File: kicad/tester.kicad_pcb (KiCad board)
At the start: 2 copper layers, 65 parts, among them J3 CONN_01X06, Q1 IRLML2402, Q2 IRLML6402, Q3 BC847, Q4 BC847, Q5 BC847, U2 NCP1450A, U3 ATMEGA328-AU, U4 LTC4054, U5 74LVC1G17, U6 SRV05, U7 XC6206P332, U8 MICRO-B_USB, Y1 16MHz

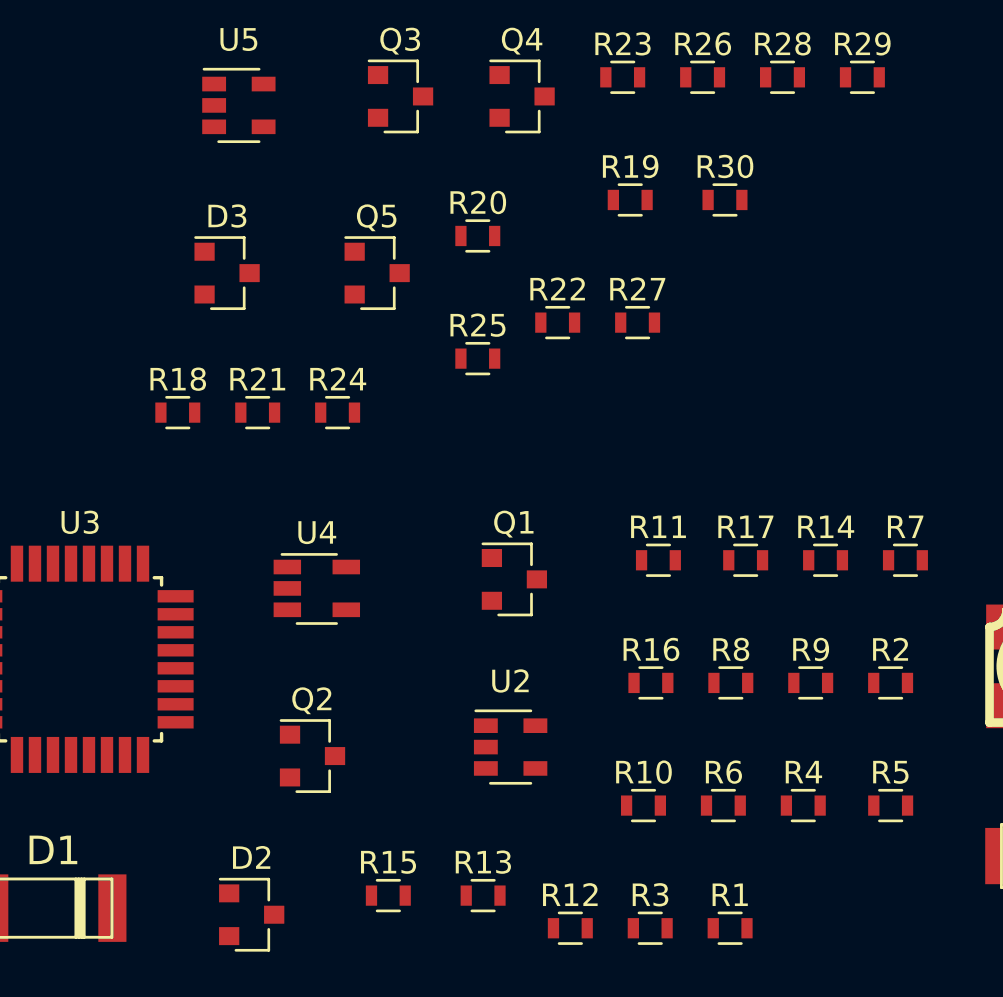
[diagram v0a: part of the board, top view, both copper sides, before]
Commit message: Change package some resistors
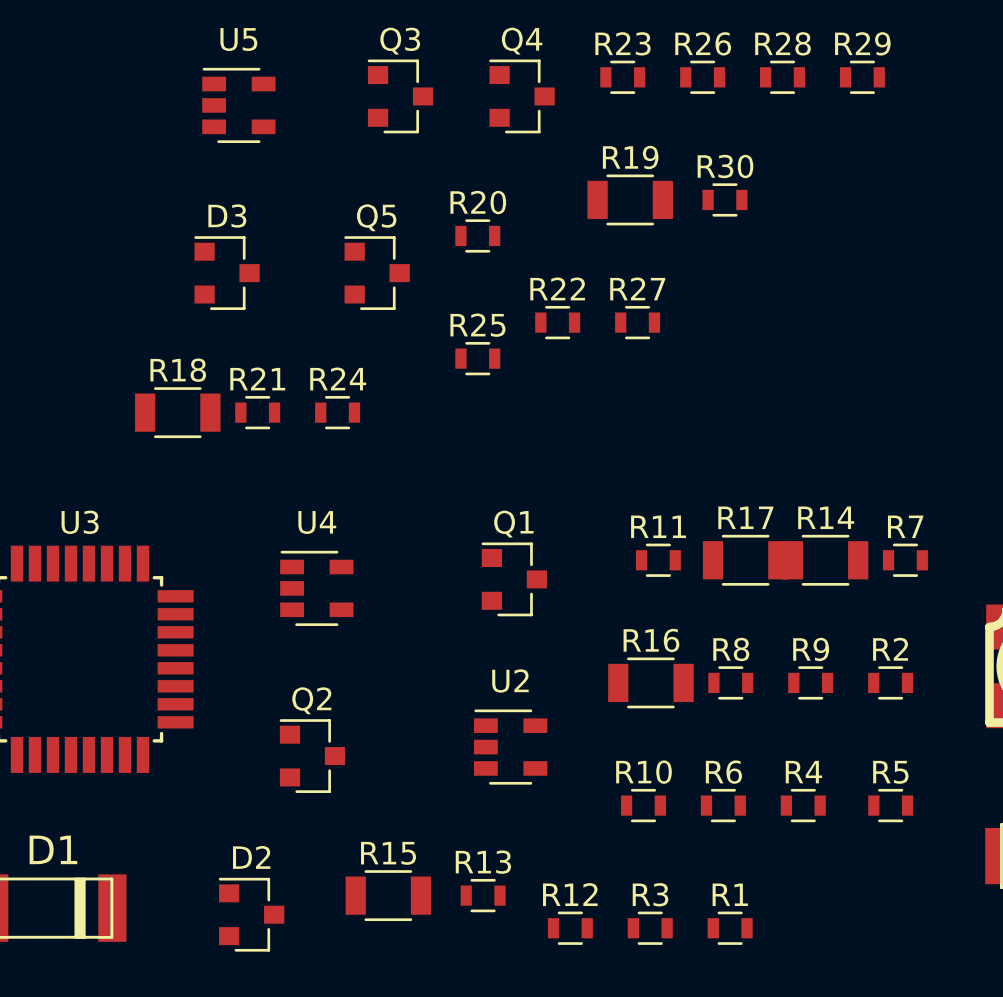
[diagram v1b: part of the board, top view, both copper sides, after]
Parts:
- R14, R15, R16, R17, R18, R19: footprint Resistors_SMD:R_0603 -> Resistors_SMD:R_1206
- U4: footprint TO_SOT_Packages_SMD:TSOT-23-5 -> TO_SOT_Packages_SMD:SOT-23-5

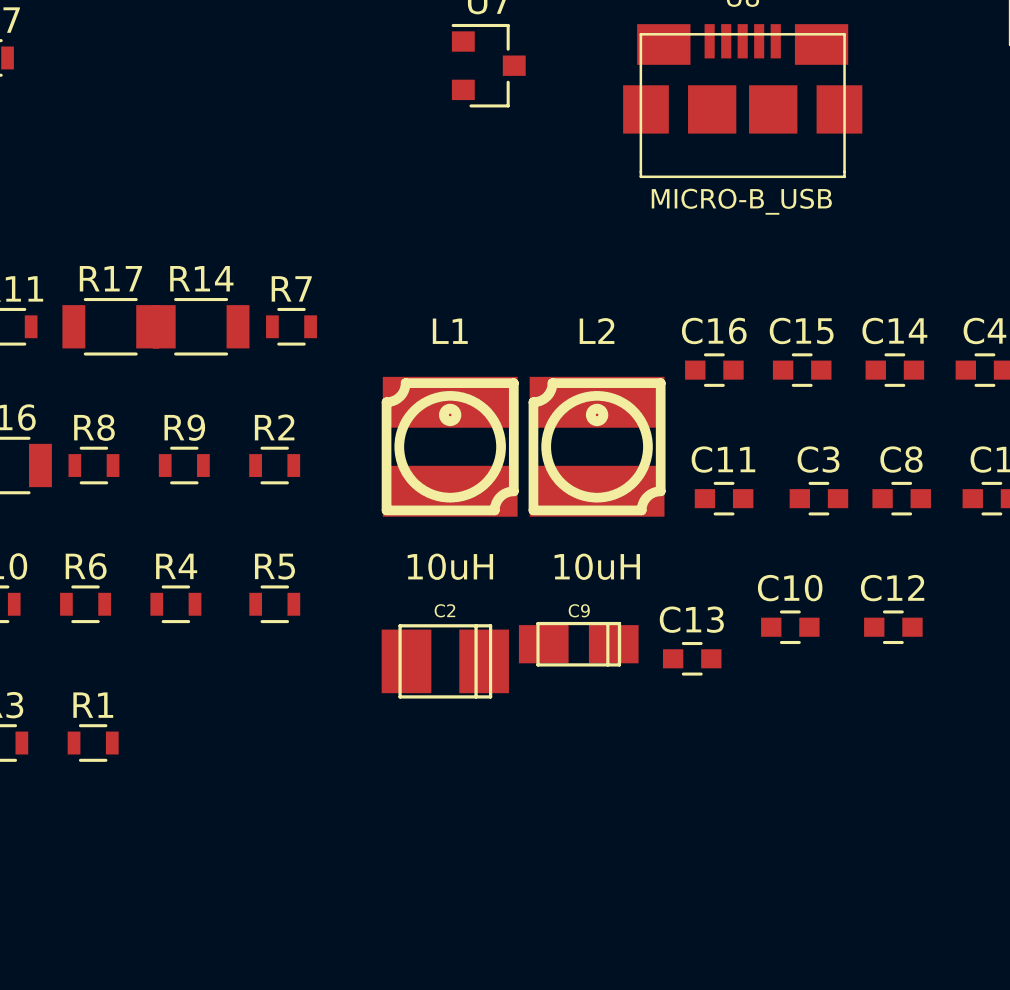
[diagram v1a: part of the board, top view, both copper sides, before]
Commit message: Add footprint oled
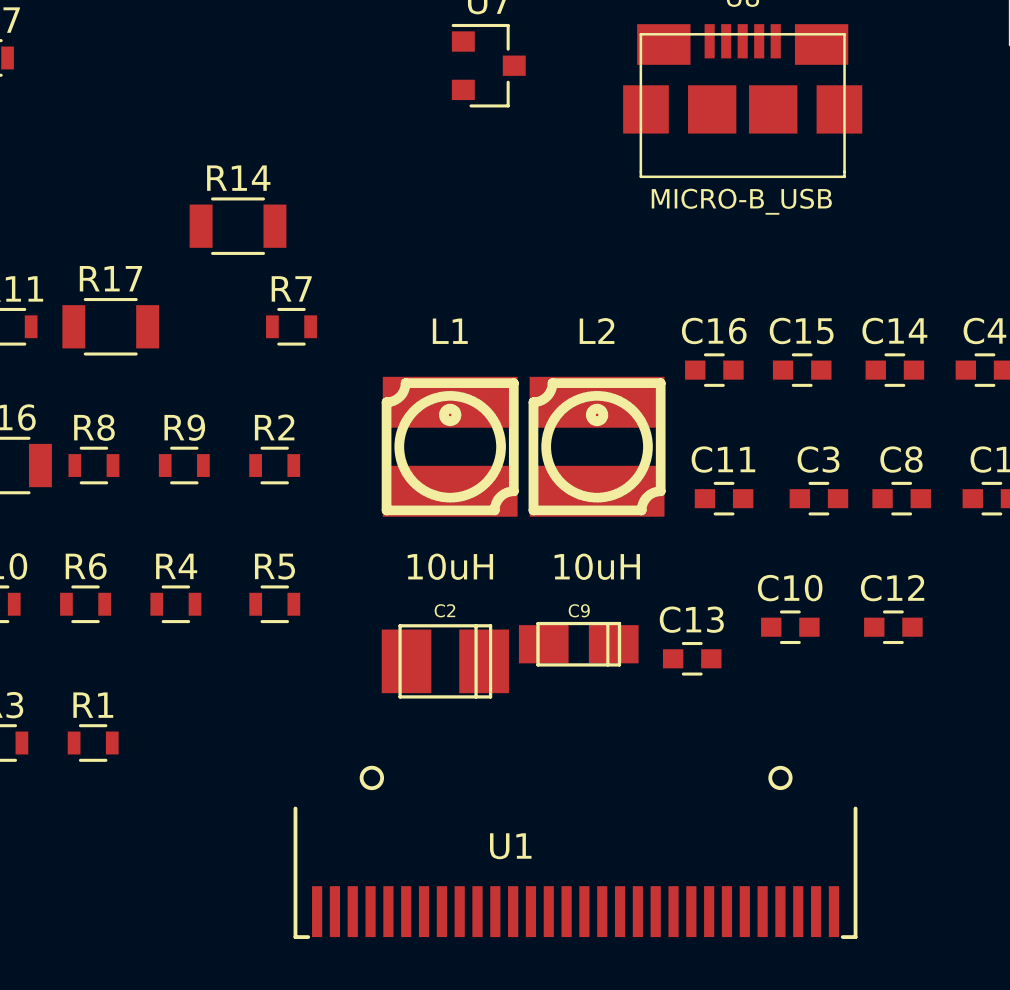
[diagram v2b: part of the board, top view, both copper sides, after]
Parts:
- added U1: OLED_128x64, tester:oled, F.Cu at (154.8, 126.0)
- moved R14 4.21 mm to (141.6, 99.1)
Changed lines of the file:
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@@
-(kicad_pcb (version 20170123) (host pcbnew no-vcs-found-f007601~58~ubuntu16.10.1)
+(kicad_pcb (version 20170123) (host pcbnew no-vcs-found-1e25c47~58~ubuntu16.10.1)
   (general
-    (links 126)
-    (no_connects 126)
-    (area 100.966391 61.86744 179.321857 122.624345)
+    (links 151)
+    (no_connects 151)
+    (area 100.966391 61.86744 179.321857 127.259001)
     (thickness 1.6)
     (drawings 0)
     (tracks 0)
     (zones 0)
-    (modules 65)
-    (nets 63)
+    (modules 66)
+    (nets 68)
   )
   (page A4)
@@
   (net 61 "Net-(C4-Pad2)")
   (net 62 "Net-(D4-Pad3)")
+  (net 63 "Net-(U1-Pad1)")
+  (net 64 "Net-(U1-Pad7)")
+  (net 65 "Net-(U1-Pad20)")
+  (net 66 "Net-(C5-Pad1)")
+  (net 67 "Net-(C6-Pad1)")
   (net_class Default "This is the default net class."
     (clearance 0.2)
@@
     (add_net "Net-(C4-Pad1)")
     (add_net "Net-(C4-Pad2)")
+    (add_net "Net-(C5-Pad1)")
+    (add_net "Net-(C6-Pad1)")
     (add_net "Net-(C7-Pad1)")
     (add_net "Net-(C8-Pad2)")
@@
     (add_net "Net-(R5-Pad2)")
     (add_net "Net-(R8-Pad2)")
+    (add_net "Net-(U1-Pad1)")
+    (add_net "Net-(U1-Pad20)")
+    (add_net "Net-(U1-Pad7)")
     (add_net "Net-(U2-Pad3)")
     (add_net "Net-(U3-Pad2)")
@@
     (add_net "Net-(U8-Pad2)")
     (add_net VCC)
+  )
+  (module tester:oled (layer F.Cu)
+    (at 154.838 125.984)
+    (fp_text reference U1 (at -2.54 -2.54) (layer F.SilkS)
+      (effects (font (size 1 1) (thickness 0.15)))
+    )
+    (fp_text value OLED_128x64 (at 4.166 -2.54) (layer F.Fab)
+      (effects (font (size 1 1) (thickness 0.15)))
+    )
+    (fp_circle (center -8 -5.25) (end -8.4 -5.2) (layer F.SilkS) (width 0.15))
+    (fp_circle (center 8.05 -5.25) (end 8.45 -5.25) (layer F.SilkS) (width 0.15))
+    (fp_line (start -11 1) (end -10.5 1) (layer F.SilkS) (width 0.15))
+    (fp_line (start -10.5 1) (end -10.5 1) (layer F.SilkS) (width 0.15))
+    (fp_line (start -11 1) (end -11 -4.05) (layer F.SilkS) (width 0.15))
+    (fp_line (start -11 -4.05) (end -11 -4.05) (layer F.SilkS) (width 0.15))
+    (fp_line (start 11 1) (end 10.5 1) (layer F.SilkS) (width 0.15))
+    (fp_line (start 10.5 1) (end 10.5 1) (layer F.SilkS) (width 0.15))
+    (fp_line (start 11 1) (end 11 -4.05) (layer F.SilkS) (width 0.15))
+    (fp_line (start 11 -4.05) (end 11 -4.05) (layer F.SilkS) (width 0.15))
+    (pad 1 smd rect (at -10.15 0) (size 0.4 2) (layers F.Cu F.Paste F.Mask)
+      (net 63 "Net-(U1-Pad1)"))
+    (pad 2 smd rect (at -9.45 0) (size 0.4 2) (layers F.Cu F.Paste F.Mask)
+      (net 59 "Net-(C3-Pad1)"))
+    (pad 3 smd rect (at -8.75 0) (size 0.4 2) (layers F.Cu F.Paste F.Mask)
+      (net 58 "Net-(C3-Pad2)"))
+    (pad 4 smd rect (at -8.05 0) (size 0.4 2) (layers F.Cu F.Paste F.Mask)
+      (net 60 "Net-(C4-Pad1)"))
+    (pad 5 smd rect (at -7.35 0) (size 0.4 2) (layers F.Cu F.Paste F.Mask)
+      (net 61 "Net-(C4-Pad2)"))
+    (pad 6 smd rect (at -6.65 0) (size 0.4 2) (layers F.Cu F.Paste F.Mask)
+      (net 56 "Net-(C16-Pad1)"))
+    (pad 7 smd rect (at -5.95 0) (size 0.4 2) (layers F.Cu F.Paste F.Mask)
+      (net 64 "Net-(U1-Pad7)"))
+    (pad 8 smd rect (at -5.25 0) (size 0.4 2) (layers F.Cu F.Paste F.Mask)
+      (net 3 GND))
+    (pad 9 smd rect (at -4.55 0) (size 0.4 2) (layers F.Cu F.Paste F.Mask)
+      (net 56 "Net-(C16-Pad1)"))
+    (pad 10 smd rect (at -3.85 0) (size 0.4 2) (layers F.Cu F.Paste F.Mask)
+      (net 3 GND))
+    (pad 11 smd rect (at -3.15 0) (size 0.4 2) (layers F.Cu F.Paste F.Mask)
+      (net 3 GND))
+    (pad 12 smd rect (at -2.45 0) (size 0.4 2) (layers F.Cu F.Paste F.Mask)
+      (net 3 GND))
+    (pad 13 smd rect (at -1.75 0) (size 0.4 2) (layers F.Cu F.Paste F.Mask)
+      (net 3 GND))
+    (pad 14 smd rect (at -1.05 0) (size 0.4 2) (layers F.Cu F.Paste F.Mask)
+      (net 21 "Net-(R1-Pad2)"))
+    (pad 15 smd rect (at -0.35 0) (size 0.4 2) (layers F.Cu F.Paste F.Mask)
+      (net 18 "Net-(R2-Pad2)"))
+    (pad 16 smd rect (at 0.35 0) (size 0.4 2) (layers F.Cu F.Paste F.Mask)
+      (net 3 GND))
+    (pad 17 smd rect (at 1.05 0) (size 0.4 2) (layers F.Cu F.Paste F.Mask)
+      (net 3 GND))
+    (pad 18 smd rect (at 1.75 0) (size 0.4 2) (layers F.Cu F.Paste F.Mask)
+      (net 17 "Net-(R3-Pad2)"))
+    (pad 19 smd rect (at 2.45 0) (size 0.4 2) (layers F.Cu F.Paste F.Mask)
+      (net 14 "Net-(R4-Pad2)"))
+    (pad 20 smd rect (at 3.15 0) (size 0.4 2) (layers F.Cu F.Paste F.Mask)
+      (net 65 "Net-(U1-Pad20)"))
+    (pad 21 smd rect (at 3.85 0) (size 0.4 2) (layers F.Cu F.Paste F.Mask)
+      (net 3 GND))
+    (pad 22 smd rect (at 4.55 0) (size 0.4 2) (layers F.Cu F.Paste F.Mask)
+      (net 3 GND))
+    (pad 23 smd rect (at 5.25 0) (size 0.4 2) (layers F.Cu F.Paste F.Mask)
+      (net 3 GND))
+    (pad 24 smd rect (at 5.95 0) (size 0.4 2) (layers F.Cu F.Paste F.Mask)
+      (net 3 GND))
+    (pad 25 smd rect (at 6.65 0) (size 0.4 2) (layers F.Cu F.Paste F.Mask)
+      (net 3 GND))
+    (pad 26 smd rect (at 7.35 0) (size 0.4 2) (layers F.Cu F.Paste F.Mask)
+      (net 22 "Net-(R5-Pad2)"))
+    (pad 27 smd rect (at 8.05 0) (size 0.4 2) (layers F.Cu F.Paste F.Mask)
+      (net 66 "Net-(C5-Pad1)"))
+    (pad 28 smd rect (at 8.75 0) (size 0.4 2) (layers F.Cu F.Paste F.Mask)
+      (net 67 "Net-(C6-Pad1)"))
+    (pad 29 smd rect (at 9.45 0) (size 0.4 2) (layers F.Cu F.Paste F.Mask)
+      (net 3 GND))
+    (pad 30 smd rect (at 10.15 0) (size 0.4 2) (layers F.Cu F.Paste F.Mask)
+      (net 3 GND))
   )
   (module Resistors_SMD:R_1206 (layer F.Cu)
@@
   )
   (module Resistors_SMD:R_1206 (layer F.Cu)
-    (at 140.131392 103.011045)
+    (at 141.581392 99.06)
     (descr "Resistor SMD 1206, reflow soldering, Vishay (see dcrcw.pdf)")
     (tags "resistor 1206")
@@
     (fp_line (start 1.6 0.8) (end -1.6 0.8) (layer F.Fab) (width 0.1))
     (fp_line (start -1.6 0.8) (end -1.6 -0.8) (layer F.Fab) (width 0.1))
-    (fp_text user %R (at 0 0) (layer F.Fab)
+    (fp_text user %R (at 0.076608 0) (layer F.Fab)
       (effects (font (size 0.7 0.7) (thickness 0.105)))
     )

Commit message: Update pcb
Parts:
- added C5: 2u2, Capacitors_SMD:C_0603, F.Cu at (160.0, 128.0)
- added C6: 2u2, Capacitors_SMD:C_0603, F.Cu at (162.1, 128.0)
- J3: footprint w_conn_jst-ph:s6b-ph-kl -> tester:avr_spi
- moved U6 113.6 mm to (63.5, 111.8)
- moved C1 85.3 mm to (90.9, 80.8)
- moved U5 74.3 mm to (180.3, 116.3), turned to 180 degrees
- moved C10 71.1 mm to (106.7, 71.8), turned to 270 degrees
- moved L1 68.3 mm to (91.9, 71.6), turned to 270 degrees
- moved C2 66.4 mm to (91.4, 84.3), turned to 180 degrees
- moved D6 63.5 mm to (119.9, 58.4), turned to 180 degrees
- moved R28 61.3 mm to (188.0, 117.3), turned to 180 degrees
- moved R25 61.2 mm to (180.3, 119.4), turned to 180 degrees
- moved R30 59.5 mm to (188.0, 115.3), turned to 180 degrees
- moved C13 58.9 mm to (103.5, 134.6), turned to 270 degrees
- moved R6 56.9 mm to (104.8, 66.0)
- moved R7 55.5 mm to (104.8, 63.5)
- moved R26 54.9 mm to (179.8, 112.8)
- moved R29 54.8 mm to (184.9, 115.3), turned to 180 degrees
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
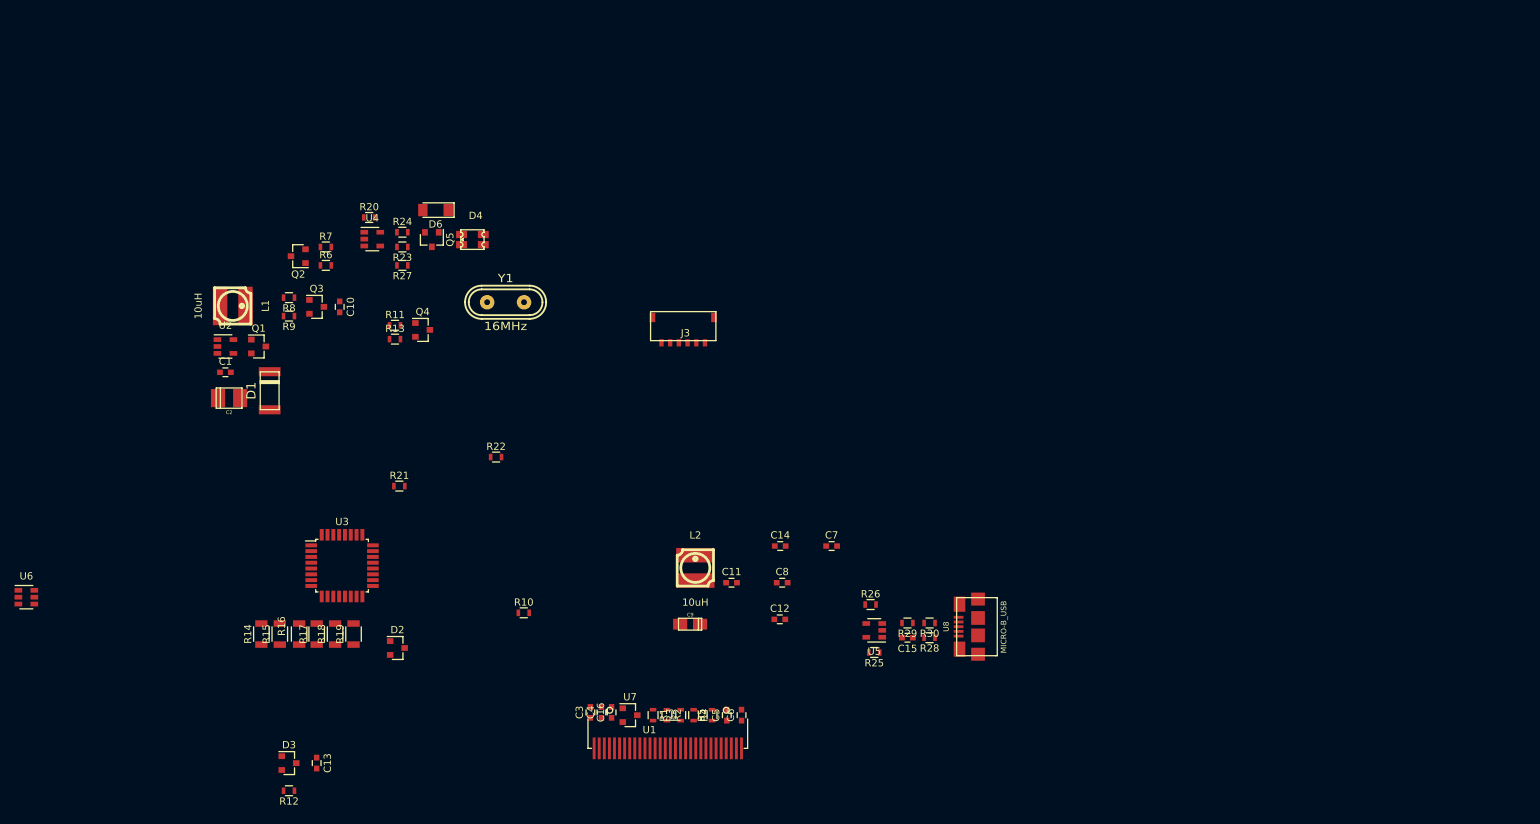
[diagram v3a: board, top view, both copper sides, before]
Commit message: Start pcb routing
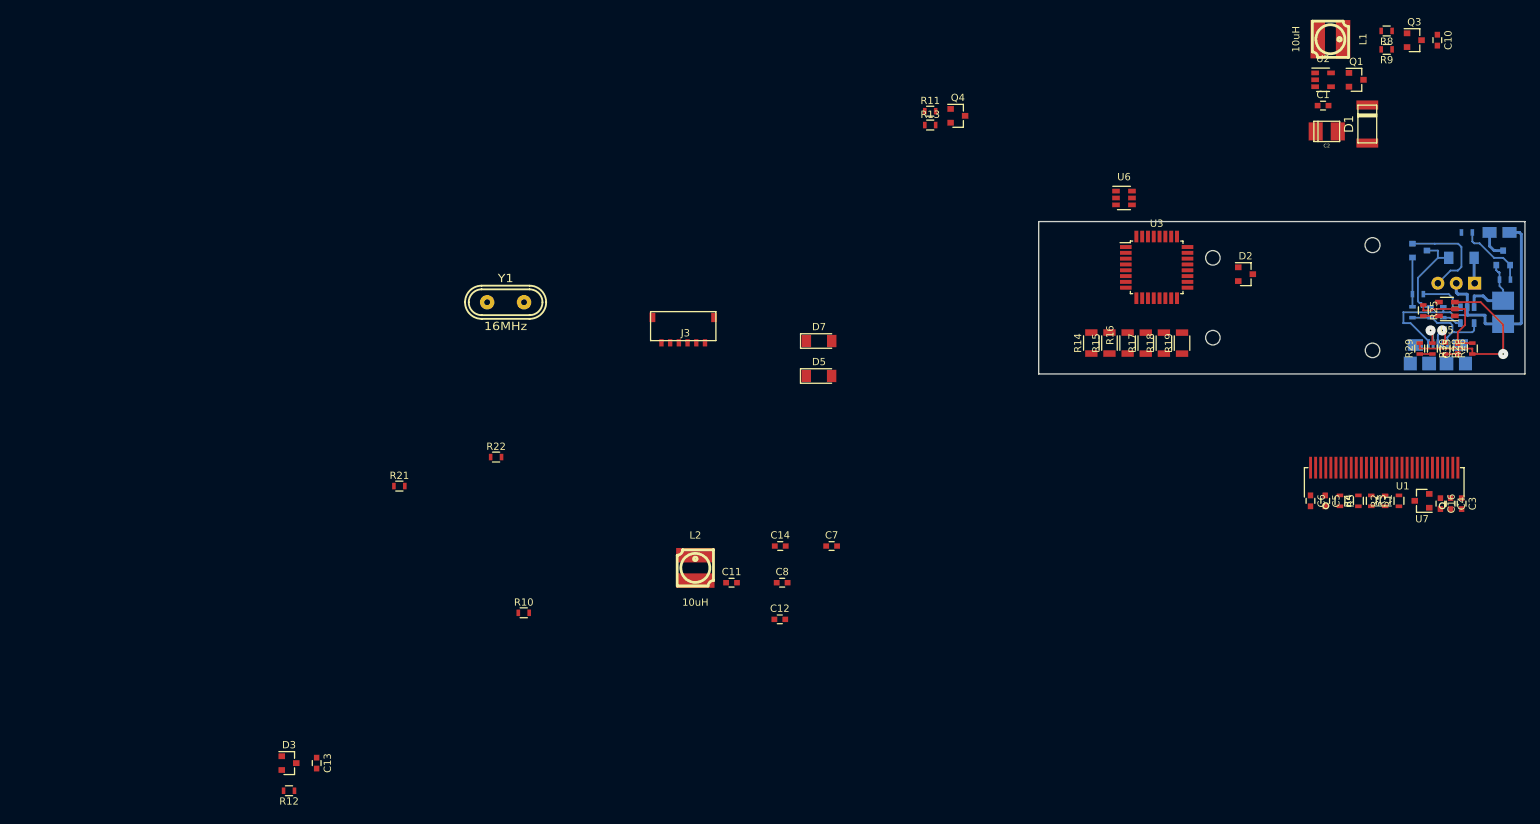
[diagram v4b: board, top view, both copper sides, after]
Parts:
- added BT1: Battery_Cell, tester:batt, B.Cu at (267.0, 72.5)
- added D5: 5V1, Diodes_SMD:D_MiniMELF_Standard, F.Cu at (172.7, 81.3)
- added D7: 5V1, Diodes_SMD:D_MiniMELF_Standard, F.Cu at (172.7, 76.5)
- C9, D6, Q2, Q5, R20, R23, R24, R27, R6, R7, U4, U8: moved to B.Cu
- D4: footprint tester:led-dual-32x27 -> LEDs:LED_D3.0mm-3; moved to B.Cu
- moved Q2 166.0 mm to (267.0, 65.0), turned to 90 degrees
- moved R7 162.5 mm to (267.2, 68.0)
- moved U6 160.9 mm to (214.8, 56.8)
- moved R6 157.3 mm to (262.0, 61.5), turned to 180 degrees
- moved C1 155.7 mm to (242.2, 44.0)
- moved R9 155.7 mm to (250.9, 36.3)
- moved C10 155.7 mm to (257.9, 35.0)
- moved C2 155.7 mm to (242.7, 47.6)
- moved D1 155.7 mm to (248.3, 46.6)
- moved L1 155.7 mm to (243.2, 34.9)
- moved Q1 155.7 mm to (246.8, 40.5)
- moved Q3 155.7 mm to (254.8, 35.0)
- moved R8 155.7 mm to (250.9, 33.7)
- moved U2 155.7 mm to (242.2, 40.5)
- moved U4 151.2 mm to (262.1, 72.9), turned to 270 degrees
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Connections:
- net Net-(BT1-Pad1) renamed /+BATT
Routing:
- net GND: track 0.00 -> 73.6 mm, vias 0 -> 1
- net Net-(D4-Pad3): track 0.00 -> 13.9 mm
- net Net-(C15-Pad2): track 0.00 -> 13.7 mm
- net Net-(D6-Pad2): track 0.00 -> 13.5 mm
- net Net-(C14-Pad1): track 0.00 -> 12.9 mm
- net /+BATT: track 0.00 -> 11.2 mm
- net Net-(Q2-Pad1): track 0.00 -> 9.85 mm
- net Net-(Q5-Pad1): track 0.00 -> 6.80 mm
- net Net-(R24-Pad1): track 0.00 -> 6.58 mm
- net Net-(R28-Pad1): track 0.00 -> 4.04 mm, vias 0 -> 1
- net /BATT_TEST: track 0.00 -> 4.01 mm
- net Net-(R30-Pad1): track 0.00 -> 3.87 mm, vias 0 -> 1
- net Net-(D4-Pad1): track 0.00 -> 3.53 mm
- net Net-(R20-Pad2): track 0.00 -> 2.66 mm
- net VCC: track 0.00 -> 2.15 mm
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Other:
- board outline added: 67 x 21 mm
- rule via_min_drill: 0.3 -> 0.2
